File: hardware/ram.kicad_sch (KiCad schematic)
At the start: 15 parts, among them U10 IS42S16320D-6BLI, U4 GateMate-CCGM1A1

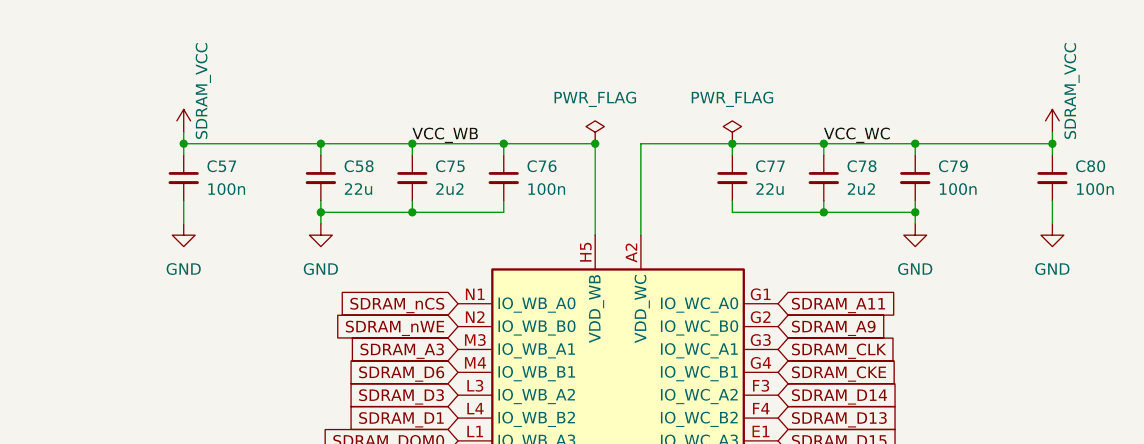
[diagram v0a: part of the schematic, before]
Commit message: power: removed rc filters from gpio domains
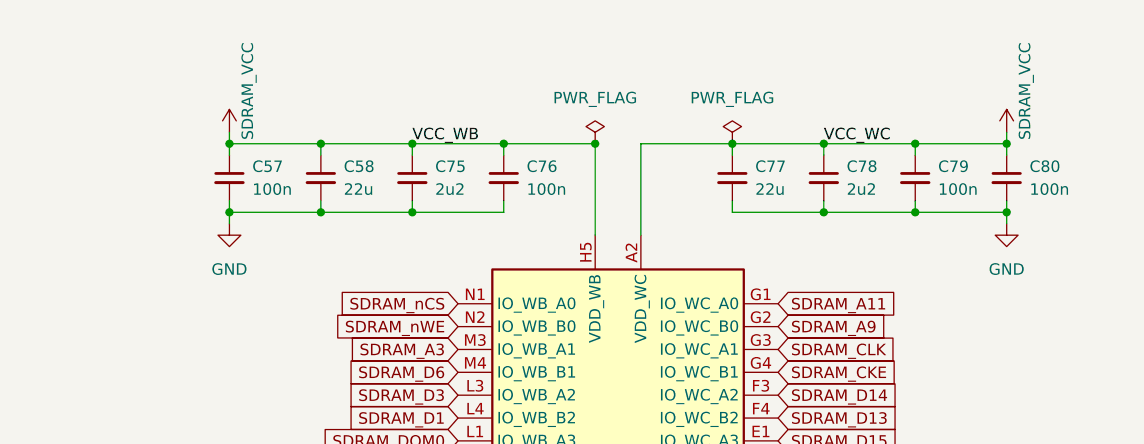
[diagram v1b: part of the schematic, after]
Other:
- moved on the sheet: C57, C80
